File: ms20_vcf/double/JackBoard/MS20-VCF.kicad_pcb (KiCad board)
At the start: 2 copper layers, 60 x 110 mm, 33 parts, among them J11 Conn_JackBoard, J12 Conn_JackBoard, J13 FilterCV2, J14 FilterIn2, J15 FilterOut2, J3 Conn_JackBoard, J4 Conn_JackBoard, J6 FilterCV1, J7 FilterIn1, J8 FilterOut1, SW1 Hpass/Lpass Switch, SW2 Bandpass, SW3 Hpass/Lpass Switch

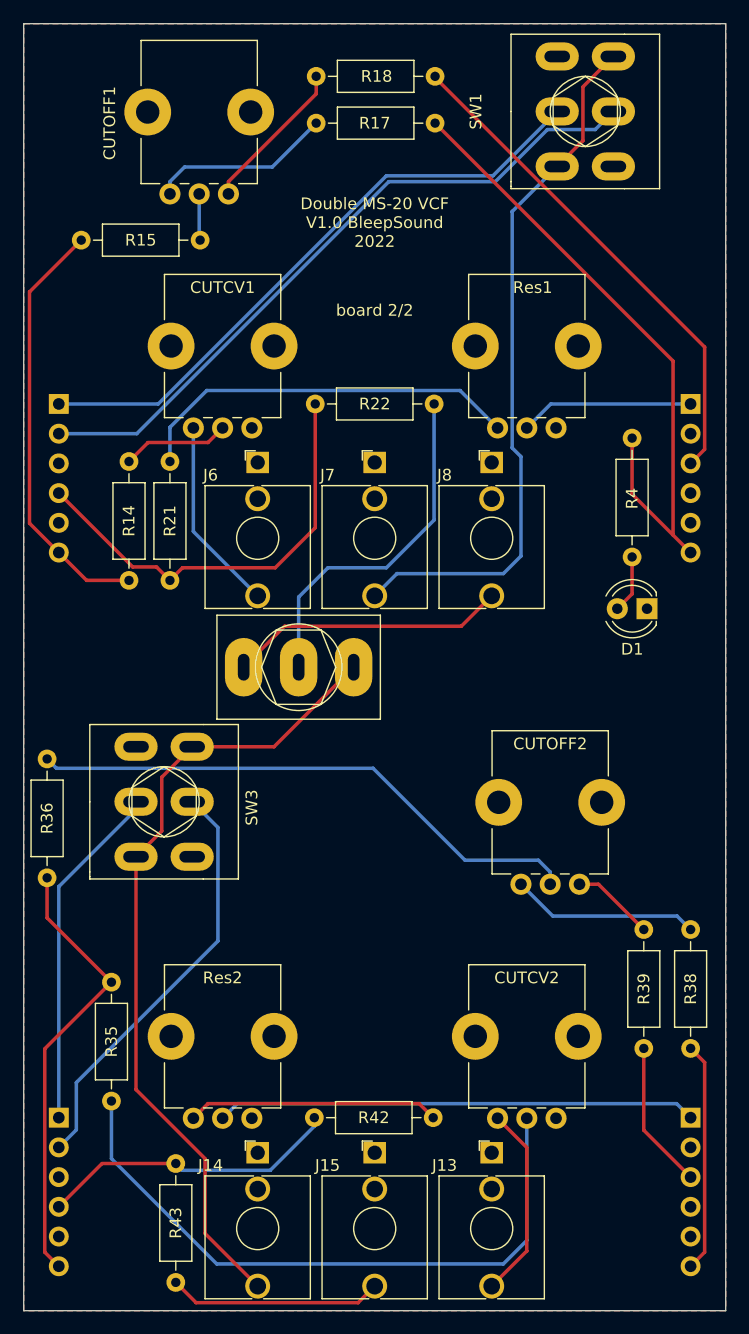
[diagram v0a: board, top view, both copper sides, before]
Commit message: updates front panel designs and gerbers before order
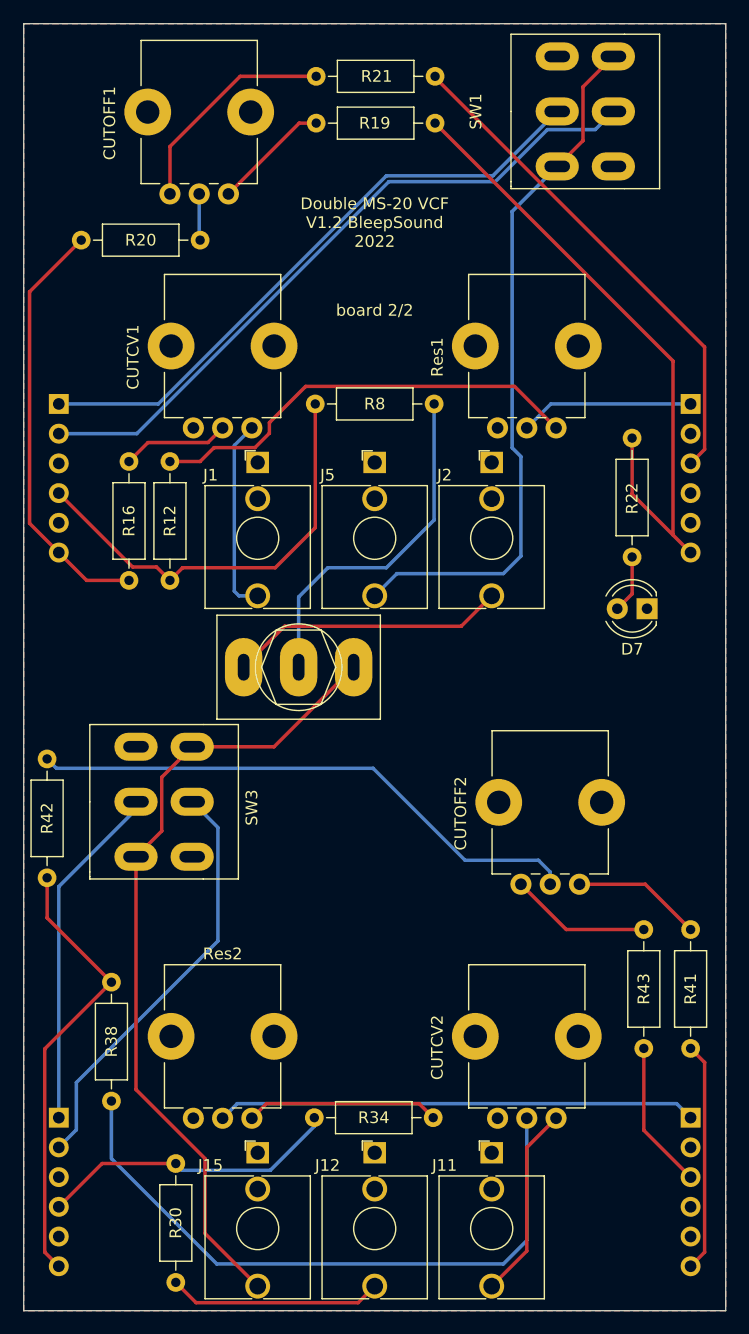
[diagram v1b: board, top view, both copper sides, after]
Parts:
- CUTCV1, CUTCV2, CUTOFF1, CUTOFF2, Res1, Res2: footprint Potentiometer_THT:Potentiometer_Bourns_PTV09A-1_Single_Vertical -> Synth:Pot-bourns-alpha
- J1: renamed from J6; footprint Connector_Audio:Jack_3.5mm_QingPu_WQP-PJ398SM_Vertical_CircularHoles -> Synth:Thonkiconn
- J11: renamed from J13; footprint Connector_Audio:Jack_3.5mm_QingPu_WQP-PJ398SM_Vertical_CircularHoles -> Synth:Thonkiconn
- J12: renamed from J15; footprint Connector_Audio:Jack_3.5mm_QingPu_WQP-PJ398SM_Vertical_CircularHoles -> Synth:Thonkiconn
- J15: renamed from J14; footprint Connector_Audio:Jack_3.5mm_QingPu_WQP-PJ398SM_Vertical_CircularHoles -> Synth:Thonkiconn
- J2: renamed from J8; footprint Connector_Audio:Jack_3.5mm_QingPu_WQP-PJ398SM_Vertical_CircularHoles -> Synth:Thonkiconn
- J5: renamed from J7; footprint Connector_Audio:Jack_3.5mm_QingPu_WQP-PJ398SM_Vertical_CircularHoles -> Synth:Thonkiconn
- renumbered D1 to D7, J11 to J10, J12 to J14, J3 to J4, J4 to J7, R21 to R12, R14 to R16, R17 to R19, R15 to R20, R18 to R21, R4 to R22, R43 to R30, R42 to R34, R35 to R38, R38 to R41, R36 to R42, R39 to R43, R22 to R8
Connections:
- CUTCV1 pad 1: GND -> /CVIn
- CUTCV1 pad 3: /CVIn -> GND
- CUTCV2 pad 1: GND -> /Filtre2/CVIn
- CUTCV2 pad 3: /Filtre2/CVIn -> GND
- CUTOFF1 pad 3: Net-(CUTOFF1-Pad3) -> Net-(R21-Pad2)
- R12 pad 1: Net-(R21-Pad1) -> Net-(R12-Pad1)
- R19 pad 1: Net-(CUTOFF1-Pad3) -> Net-(CUTOFF1-Pad1)
- R21 pad 2: Net-(CUTOFF1-Pad1) -> Net-(R21-Pad2)
- R34 pad 1: Net-(R42-Pad1) -> Net-(R34-Pad1)
- R41 pad 1: Net-(CUTOFF2-Pad3) -> Net-(CUTOFF2-Pad1)
- R43 pad 2: Net-(CUTOFF2-Pad1) -> Net-(CUTOFF2-Pad3)
- Res1 pad 1: GND -> Net-(R12-Pad1)
- Res1 pad 3: Net-(R21-Pad1) -> GND
- Res2 pad 1: GND -> Net-(R34-Pad1)
- Res2 pad 3: Net-(R42-Pad1) -> GND
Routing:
- net Net-(R12-Pad1): track 0.00 -> 37.7 mm
- net Net-(R21-Pad1): track 33.5 -> 0.00 mm
- net Net-(R42-Pad1): track 21.5 -> 0.00 mm
- net Net-(R21-Pad2): track 0.00 -> 19.0 mm
- net Net-(R34-Pad1): track 0.00 -> 16.5 mm
- net Net-(CUTOFF1-Pad3): track 15.6 -> 0.00 mm
- net Net-(CUTOFF2-Pad3): track 16.1 -> 12.1 mm
- net Net-(CUTOFF2-Pad1): track 7.10 -> 11.1 mm
- net Net-(CUTOFF1-Pad1): track 13.2 -> 10.0 mm
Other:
- board text added: "Double MS-20 VCF V1.2 BleepSound 2022"
- board text removed: "Double MS-20 VCF V1.0 BleepSound 2022"
